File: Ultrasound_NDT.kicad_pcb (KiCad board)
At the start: 4 copper layers, 396 parts, among them J1 Conn_01x02_Pin, J10 CONSMA002-SMD, J11 Logger Connector, J12 UART Connector, J13 External UART, J14 External I2C, J15 JTAG Header, J16 External Power Connector, J17 Input Power, J18 Conn_01x02_Pin, J19 Conn_01x02_Pin, J2 Conn_01x02_Pin, J20 Conn_01x02_Pin, J21 Conn_01x02_Pin, J22 Conn_01x02_Pin, J23 Conn_01x02_Pin, J24 Conn_01x02_Pin, J25 Conn_01x02_Pin, J26 Spectrography Power, J27 Conn_01x02_Pin, J3 CONSMA002-SMD, J4 CONSMA002-SMD, J5 CONSMA002-SMD, J6 CONSMA002-SMD, J7 CONSMA002-SMD, J8 CONSMA002-SMD, J9 CONSMA002-SMD, SW1 XRSn_button, U1 AD8334ACPZ, U10 TLV9354IDR, U11 TLV9354IDR, U12 TPS63700DRCR, U13 M24M01E-FMN6TP, U14 LDL212PU50R, U15 AZ1117CH2-3.3, U16 AZ1117CH2-3.3, U17 TRS3221EIPWR, U2 DSC1001DI2-125.0000T, U3 MAX14808ETK_, U4 AD8334ACPZ, U5 F280025PNS, U6 REF3030, U7 MIC920YC5-TR, U8 TLV9354IDR, U9 TLV9354IDR, Y2 H130B-16.000-18-3030-EXT-TR

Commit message: finished 70% of the layout, only power is remaining + matching parts with each other (analog)
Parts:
- removed TP1, TP17, TP18, TP19, TP2, TP20, TP21, TP22, TP23, TP24, TP25, TP26, TP27, TP28, TP29, TP3, TP30, TP31, TP32, TP33, TP34, TP35, TP36, TP37, TP38, TP39, TP4, TP40, TP41, TP42, TP43, TP44, TP45, TP46, TP47, TP48, TP49, TP5, TP50, TP51, TP52, TP53, TP54, TP55, TP56, TP57, TP58, TP59, TP6, TP60, TP61, TP62, TP63, TP64, TP65, TP66, TP67, TP68, TP69, TP7, TP70, TP71, TP72, TP73, TP74, TP75, TP76, TP77, TP78, TP79, TP8, TP80, TP81: RCT-0C, digikey-footprints:PROBE_PAD_0805
- removed TP10, TP11, TP12, TP13, TP14, TP15, TP16, TP9: TestPoint, TestPoint:TestPoint_Pad_D1.5mm
- C10, C11, C112, C113, C12, C13, C16, C17, C18, C19, C2, C20, C21, C22, C23, C24, C25, C29, C3, C31, C32, C33, C34, C35, C36, C37, C38, C39, C4, C40, C41, C42, C43, C44, C45, C46, C5, C57, C6, C60, C63, C66, C69, C7, C72, C73, C74, C8, C9: moved to B.Cu
- moved C68 289.4 mm to (169.8, 241.5), turned to 90 degrees
- moved C66 287.1 mm to (172.2, 215.4), turned to 90 degrees
- moved C63 286.6 mm to (171.7, 212.4), turned to -90 degrees
- moved C74 283.1 mm to (170.2, 217.6), turned to 90 degrees
- moved R41 282.7 mm to (167.8, 241.7), turned to -90 degrees
- moved C73 282.5 mm to (169.7, 214.4), turned to -45 degrees
- moved C67 281.9 mm to (161.0, 242.4), turned to 90 degrees
- moved R40 275.4 mm to (159.0, 242.6), turned to -90 degrees
- moved C57 272.3 mm to (155.5, 215.4), turned to 90 degrees
- moved C69 271.9 mm to (157.7, 217.9), turned to 90 degrees
- moved C60 271.6 mm to (156.0, 212.3), turned to -90 degrees
- moved C72 271.2 mm to (158.0, 214.6), turned to -135 degrees
- moved R104 269.1 mm to (171.0, 223.1), turned to 180 degrees
- moved R42 265.6 mm to (156.0, 223.1)
- moved R43 264.7 mm to (156.0, 221.6)
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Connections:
- J15 pad 4: /Main MCU Section/JTAG_TDO -> /Main MCU Section/JTAG_TMS
- J15 pad 5: /Main MCU Section/JTAG_TCK -> /Main MCU Section/JTAG_TDO
- J15 pad 6: /Main MCU Section/JTAG_TMS -> /Main MCU Section/JTAG_TCK
- R10 pad 1: /Main MCU Section/CH7_A -> /Main MCU Section/CH7_A_MCU
- R11 pad 1: /Main MCU Section/CH5_A -> /Main MCU Section/CH5_A_MCU
- R12 pad 1: /Main MCU Section/CH1_A -> /Main MCU Section/CH1_A_MCU
- R13 pad 1: /Main MCU Section/CH1_B -> /Main MCU Section/CH1_B_MCU
- R14 pad 1: /Main MCU Section/CH2_A -> /Main MCU Section/CH2_A_MCU
- R15 pad 1: /Main MCU Section/CH2_B -> /Main MCU Section/CH2_B_MCU
- R16 pad 1: /Main MCU Section/CH3_A -> /Main MCU Section/CH3_A_MCU
- R17 pad 1: /Main MCU Section/CH3_B -> /Main MCU Section/CH3_B_MCU
- R18 pad 1: /Main MCU Section/CH4_A -> /Main MCU Section/CH4_A_MCU
- R19 pad 1: /Main MCU Section/CH4_B -> /Main MCU Section/CH4_B_MCU
- R4 pad 1: /Main MCU Section/CH5_B -> /Main MCU Section/CH5_B_MCU
- R5 pad 1: /Main MCU Section/CH8_B -> /Main MCU Section/CH8_B_MCU
- R6 pad 1: /Main MCU Section/CH6_A -> /Main MCU Section/CH6_A_MCU
- R7 pad 1: /Main MCU Section/CH6_B -> /Main MCU Section/CH6_B_MCU
- R8 pad 1: /Main MCU Section/CH8_A -> /Main MCU Section/CH8_A_MCU
- R9 pad 1: /Main MCU Section/CH7_B -> /Main MCU Section/CH7_B_MCU
- U5 pad 62: /Main MCU Section/CH5_A -> /Main MCU Section/CH5_A_MCU
- U5 pad 63: /Main MCU Section/CH5_B -> /Main MCU Section/CH5_B_MCU
- U5 pad 64: /Main MCU Section/CH6_A -> /Main MCU Section/CH6_A_MCU
- U5 pad 65: /Main MCU Section/CH6_B -> /Main MCU Section/CH6_B_MCU
- U5 pad 66: /Main MCU Section/CH7_A -> /Main MCU Section/CH7_A_MCU
- U5 pad 67: /Main MCU Section/CH7_B -> /Main MCU Section/CH7_B_MCU
- U5 pad 68: /Main MCU Section/CH8_A -> /Main MCU Section/CH8_A_MCU
- U5 pad 69: /Main MCU Section/CH8_B -> /Main MCU Section/CH8_B_MCU
- U5 pad 73: /Main MCU Section/CH4_B -> /Main MCU Section/CH4_B_MCU
- U5 pad 74: /Main MCU Section/CH4_A -> /Main MCU Section/CH4_A_MCU
- U5 pad 75: /Main MCU Section/CH3_B -> /Main MCU Section/CH3_B_MCU
- U5 pad 76: /Main MCU Section/CH3_A -> /Main MCU Section/CH3_A_MCU
- U5 pad 77: /Main MCU Section/CH2_B -> /Main MCU Section/CH2_B_MCU
- U5 pad 78: /Main MCU Section/CH2_A -> /Main MCU Section/CH2_A_MCU
- U5 pad 79: /Main MCU Section/CH1_B -> /Main MCU Section/CH1_B_MCU
- U5 pad 80: /Main MCU Section/CH1_A -> /Main MCU Section/CH1_A_MCU

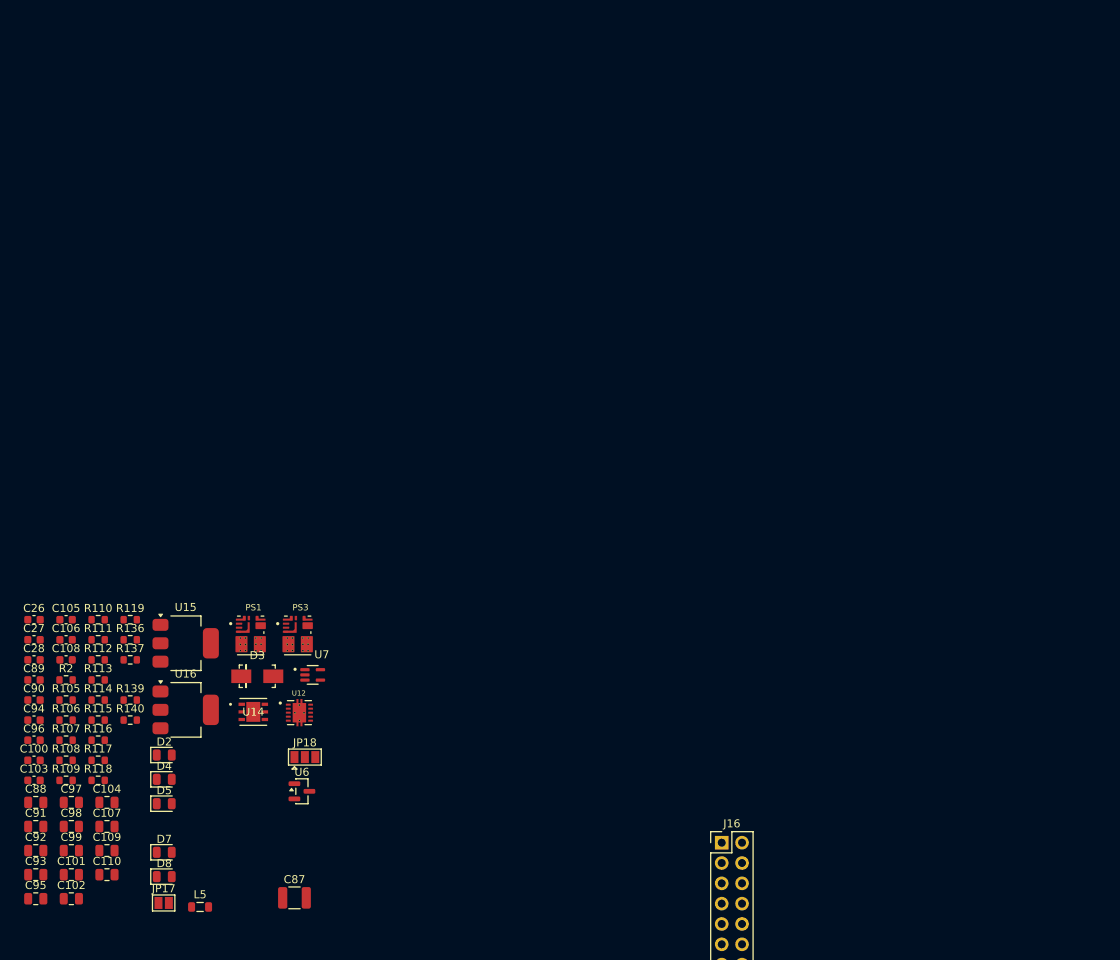
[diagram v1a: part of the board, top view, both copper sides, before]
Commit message: finished laying out all individual blocks, integration comes next, updated schematic
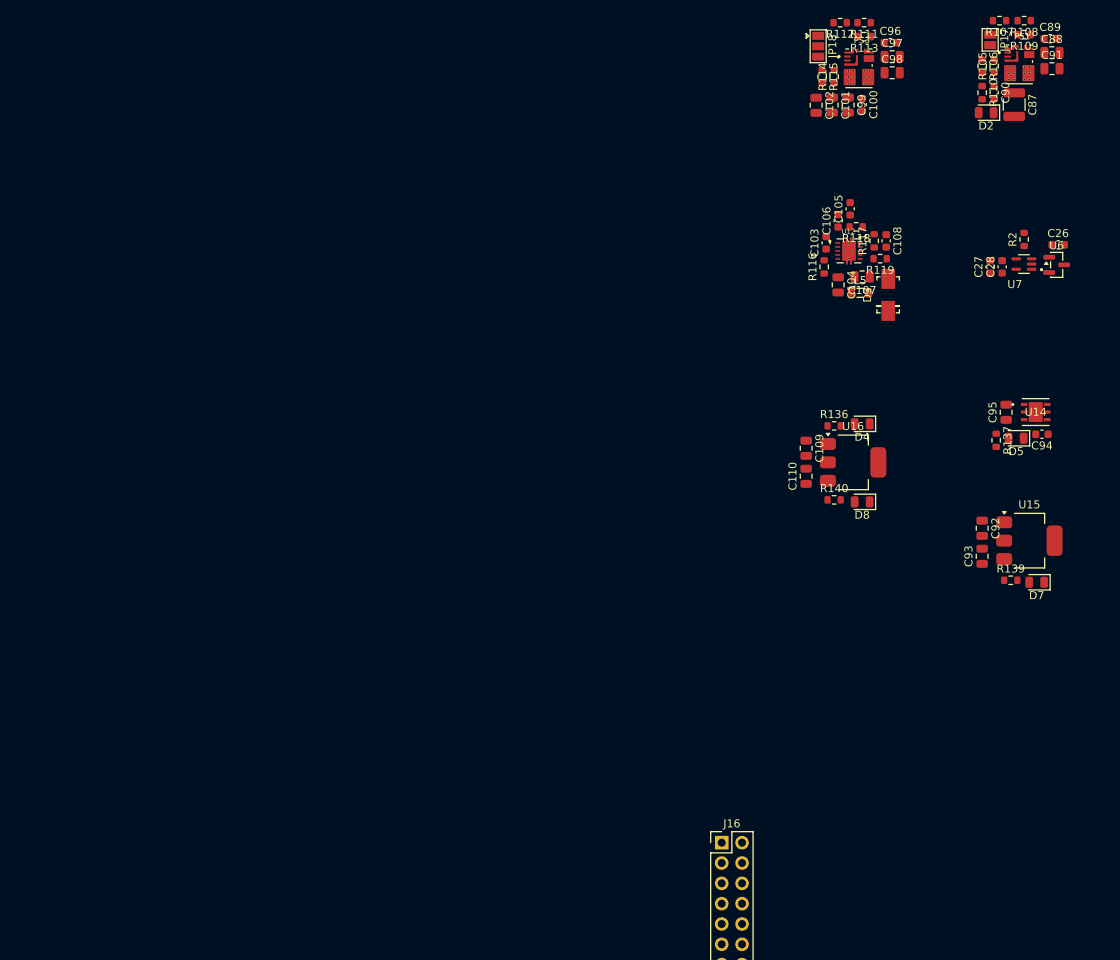
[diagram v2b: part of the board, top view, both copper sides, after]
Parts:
- moved C91 158.5 mm to (-30.8, 24.0)
- moved C88 157.9 mm to (-30.8, 22.0)
- moved R109 151.8 mm to (-34.2, 19.8), turned to 180 degrees
- moved R108 151.3 mm to (-34.2, 18.0), turned to 180 degrees
- moved C89 150.2 mm to (-31.0, 20.2)
- moved JP17 149.4 mm to (-38.5, 20.4), turned to -90 degrees
- moved R107 147.3 mm to (-37.3, 18.0), turned to 180 degrees
- moved C90 142.0 mm to (-38.0, 27.0), turned to -90 degrees
- moved R106 140.7 mm to (-39.5, 23.7), turned to -90 degrees
- moved R105 140.5 mm to (-38.0, 23.7), turned to 90 degrees
- moved C98 139.3 mm to (-50.8, 24.5)
- moved C97 138.6 mm to (-50.8, 22.5)
- moved C96 138.1 mm to (-51.0, 20.8)
- moved C26 136.3 mm to (-30.0, 46.0)
- moved C102 136.0 mm to (-60.2, 28.6), turned to -90 degrees
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
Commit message: fininshed 90% placement, only power section needs refinement, next sprint the stackup will be decided, probably 6 layers
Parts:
- C100, C101, C102, C103, C104, C105, C106, C107, C108, C109, C110, C26, C27, C28, C87, C88, C89, C90, C91, C92, C93, C94, C95, C96, C97, C98, C99, D2, D3, D4, D5, D6, D7, D8, J17, J26, JP17, JP18, L5, PS1, PS3, R10, R105, R106, R107, R108, R109, R11, R110, R111, R112, R113, R114, R115, R116, R117, R118, R119, R12, R128, R129, R13, R130, R131, R132, R133, R134, R135, R136, R137, R138, R139, R14, R140, R15, R16, R17, R18, R19, R2, R4, R5, R6, R7, R8, R9, U12, U14, U15, U16, U6, U7: moved to B.Cu
- moved J17 259.7 mm to (116.1, 173.8), turned to 180 degrees
- moved D6 253.4 mm to (122.4, 167.0), turned to 180 degrees
- moved J26 250.3 mm to (115.1, 167.0), turned to 90 degrees
- moved R138 249.5 mm to (118.9, 167.0)
- moved R111 219.4 mm to (109.4, 164.4)
- moved R112 219.4 mm to (106.4, 164.4)
- moved R113 217.1 mm to (109.4, 162.7)
- moved C96 216.1 mm to (112.6, 161.9)
- moved JP18 215.5 mm to (103.6, 161.5), turned to 90 degrees
- moved R107 214.5 mm to (119.3, 164.5)
- moved R108 214.5 mm to (122.4, 164.5)
- moved C97 213.9 mm to (112.9, 160.2)
- moved R109 212.1 mm to (122.4, 162.8)
- moved PS3 212.0 mm to (108.7, 158.7)
- moved C89 211.4 mm to (125.6, 162.3)
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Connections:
- C35 pad 1: /Receiving Section/TR_OUT1 -> /Receiving Section/TR_OUT4
- C36 pad 1: /Receiving Section/TR_OUT2 -> /Receiving Section/TR_OUT1
- C37 pad 1: /Receiving Section/TR_OUT3 -> /Receiving Section/TR_OUT2
- C38 pad 1: /Receiving Section/TR_OUT4 -> /Receiving Section/TR_OUT3
- C57 pad 1: /Receiving Section/TR_OUT5 -> /Receiving Section/TR_OUT8
- C60 pad 1: /Receiving Section/TR_OUT6 -> /Receiving Section/TR_OUT5
- C63 pad 1: /Receiving Section/TR_OUT7 -> /Receiving Section/TR_OUT6
- C66 pad 1: /Receiving Section/TR_OUT8 -> /Receiving Section/TR_OUT7
- J15 pad 4: /Main MCU Section/JTAG_TMS -> /Main MCU Section/JTAG_TDO
- J15 pad 5: /Main MCU Section/JTAG_TDO -> /Main MCU Section/JTAG_TCK
- J15 pad 6: /Main MCU Section/JTAG_TCK -> /Main MCU Section/JTAG_TMS
- R32 pad 1: /Receiving Section/TR_OUT4 -> /Receiving Section/TR_OUT3
- R33 pad 1: /Receiving Section/TR_OUT3 -> /Receiving Section/TR_OUT2
- R34 pad 1: /Receiving Section/TR_OUT2 -> /Receiving Section/TR_OUT1
- R35 pad 1: /Receiving Section/TR_OUT1 -> /Receiving Section/TR_OUT4
- R44 pad 1: /Receiving Section/TR_OUT8 -> /Receiving Section/TR_OUT7
- R45 pad 1: /Receiving Section/TR_OUT7 -> /Receiving Section/TR_OUT6
- R46 pad 1: /Receiving Section/TR_OUT6 -> /Receiving Section/TR_OUT5
- R47 pad 1: /Receiving Section/TR_OUT5 -> /Receiving Section/TR_OUT8
- U1 pad 1: /Receiving Section/TR_OUT6 -> /Receiving Section/TR_OUT5
- U1 pad 16: /Receiving Section/TR_OUT7 -> /Receiving Section/TR_OUT6
- U1 pad 19: /Receiving Section/TR_OUT8 -> /Receiving Section/TR_OUT7
- U1 pad 62: /Receiving Section/TR_OUT5 -> /Receiving Section/TR_OUT8
- U4 pad 1: /Receiving Section/TR_OUT2 -> /Receiving Section/TR_OUT1
- U4 pad 16: /Receiving Section/TR_OUT3 -> /Receiving Section/TR_OUT2
- U4 pad 19: /Receiving Section/TR_OUT4 -> /Receiving Section/TR_OUT3
- U4 pad 62: /Receiving Section/TR_OUT1 -> /Receiving Section/TR_OUT4
- U5 pad 69: /Main MCU Section/CH8_B_MCU -> /Main MCU Section/CH8_B
- U5 pad 73: /Main MCU Section/CH4_B_MCU -> /Main MCU Section/CH4_B
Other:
- board text added: "Split this header into 2 separate headers."

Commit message: Finished placement & started routing, check on stackup & see routing & sigal integrity videos downloaded
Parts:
- added J28: Conn_02x04_Odd_Even, Connector_PinHeader_2.54mm:PinHeader_2x04_P2.54mm_Vertical, F.Cu at (127.0, 61.4)
- C47, C48, C67, C68, L1, L2, L3, L4, R38, R39, R40, R41: moved to B.Cu
- J16: value External Power Connector -> Conn_02x04_Odd_Even; footprint Connector_PinHeader_2.54mm:PinHeader_2x08_P2.54mm_Vertical -> Connector_PinHeader_2.54mm:PinHeader_2x04_P2.54mm_Vertical
- moved J17 119.6 mm to (64.8, 65.8), turned to 90 degrees
- moved R112 110.1 mm to (70.6, 60.4), turned to 90 degrees
- moved R111 108.3 mm to (70.6, 63.4), turned to 90 degrees
- moved JP18 108.2 mm to (73.5, 57.6), turned to 0 degrees
- moved J26 107.8 mm to (65.0, 71.6), turned to 180 degrees
- moved R138 107.1 mm to (68.0, 72.9), turned to -90 degrees
- moved R113 106.0 mm to (72.3, 63.4), turned to 90 degrees
- moved D6 105.8 mm to (68.0, 76.4), turned to 90 degrees
- moved R115 104.6 mm to (77.3, 56.1), turned to 0 degrees
- moved R107 103.5 mm to (70.5, 73.3), turned to 90 degrees
- moved R114 103.5 mm to (77.3, 57.6), turned to 180 degrees
- moved C96 103.2 mm to (73.1, 66.6), turned to -90 degrees
- moved R108 102.3 mm to (70.5, 76.4), turned to 90 degrees
- moved C110 102.2 mm to (82.0, 52.1), turned to -90 degrees
- moved C101 101.9 mm to (77.6, 59.4), turned to 180 degrees
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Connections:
- R128 pad 2: /Receiving Section/TR_OUT6 -> /Receiving Section/TR_OUT8
- R130 pad 2: /Receiving Section/TR_OUT2 -> /Receiving Section/TR_OUT4
- R133 pad 1: /Receiving Section/TR_OUT4 -> /Receiving Section/TR_OUT2
- R135 pad 1: /Receiving Section/TR_OUT8 -> /Receiving Section/TR_OUT6
- R85 pad 2: /Pulsing Section/TR2 -> /Pulsing Section/TR4
- R87 pad 2: /Pulsing Section/TR4 -> /Pulsing Section/TR2
- R92 pad 2: /Pulsing Section/TR6 -> /Pulsing Section/TR8
- R97 pad 2: /Pulsing Section/TR8 -> /Pulsing Section/TR6
- U5 pad 1: /Main MCU Section/AFE_GAIN_B1 -> /Main MCU Section/AFE_GAIN_A2
- U5 pad 10: /Main MCU Section/ADC1 -> /Main MCU Section/ADC3
- U5 pad 12: /Main MCU Section/ADC3 -> /Main MCU Section/ADC1
- U5 pad 14: /Main MCU Section/ADC5 -> /Main MCU Section/ADC8
- U5 pad 15: /Main MCU Section/ADC6 -> /Main MCU Section/ADC7
- U5 pad 16: /Main MCU Section/ADC7 -> /Main MCU Section/ADC6
- U5 pad 17: /Main MCU Section/ADC8 -> /Main MCU Section/ADC5
- U5 pad 2: /Main MCU Section/AFE_GAIN_B2 -> /Main MCU Section/AFE_GAIN_A1
- U5 pad 58: /Main MCU Section/AFE_GAIN_A2 -> /Main MCU Section/AFE_GAIN_B2
- U5 pad 59: /Main MCU Section/AFE_GAIN_A1 -> /Main MCU Section/AFE_GAIN_B1
- U5 pad 69: /Main MCU Section/CH8_B -> /Main MCU Section/CH8_B_MCU
- U5 pad 73: /Main MCU Section/CH4_B -> /Main MCU Section/CH4_B_MCU
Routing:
- net /Main MCU Section/CH5_A_MCU: track 0.00 -> 13.4 mm
- net /Main MCU Section/CH5_B_MCU: track 0.00 -> 12.4 mm
- net /Main MCU Section/CH1_A_MCU: track 0.00 -> 11.7 mm
- net /Main MCU Section/CH6_A_MCU: track 0.00 -> 11.3 mm
- net /Main MCU Section/CH1_B_MCU: track 0.00 -> 10.9 mm
- net /Main MCU Section/CH2_A_MCU: track 0.00 -> 10.2 mm
- net /Main MCU Section/CH6_B_MCU: track 0.00 -> 9.75 mm
- net /Main MCU Section/CH2_B_MCU: track 0.00 -> 9.38 mm
- net /Main MCU Section/CH7_A_MCU: track 0.00 -> 9.00 mm
- net /Main MCU Section/CH3_A_MCU: track 0.00 -> 8.82 mm
- net /Main MCU Section/CH7_B_MCU: track 0.00 -> 7.86 mm
- net /Main MCU Section/CH3_B_MCU: track 0.00 -> 7.75 mm
- net /Main MCU Section/CH8_A_MCU: track 0.00 -> 7.44 mm
- net /Main MCU Section/CH4_A_MCU: track 0.00 -> 7.34 mm
- net /Main MCU Section/CH4_B_MCU: track 0.00 -> 7.17 mm
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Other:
- board outline added: 100 x 100 mm
- copper layers 4 -> 6
- board text removed: "Split this header into 2 separate headers."

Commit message: started routing, finished 15%
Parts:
- C115, R49, R50: moved to B.Cu
- R10, R11, R12, R13, R14, R15, R16, R17, R18, R19, R4, R5, R6, R7, R8, R9: moved to F.Cu
- moved R49 7.55 mm to (112.2, 76.2), turned to -90 degrees
- moved R50 7.05 mm to (113.8, 76.2), turned to -90 degrees
- moved C14 4.72 mm to (128.5, 99.2), turned to 0 degrees
- moved R11 4.26 mm to (121.8, 80.8)
- moved R12 4.20 mm to (104.0, 80.8)
- moved R20 3.54 mm to (153.0, 111.0), turned to 90 degrees
- moved R6 3.48 mm to (119.8, 80.8)
- moved R14 3.41 mm to (106.0, 80.8)
- moved R13 3.07 mm to (105.0, 83.8)
- moved R4 3.05 mm to (120.8, 83.8)
- moved R22 2.96 mm to (153.0, 114.2), turned to -90 degrees
- moved R10 2.85 mm to (117.8, 80.8)
- moved R16 2.77 mm to (108.0, 80.8)
- moved R1 2.69 mm to (125.4, 99.2), turned to 0 degrees
- moved R8 2.48 mm to (115.8, 80.8)
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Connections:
- J15 pad 4: /Main MCU Section/JTAG_TDO -> /Main MCU Section/JTAG_TMS
- J15 pad 5: /Main MCU Section/JTAG_TCK -> /Main MCU Section/JTAG_TDO
- J15 pad 6: /Main MCU Section/JTAG_TMS -> /Main MCU Section/JTAG_TCK
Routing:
- net /Main MCU Section/LINB_RX: track 0.00 -> 47.3 mm
- net /Main MCU Section/JTAG_TDO: track 0.00 -> 45.9 mm, vias 0 -> 1
- net /Pulsing Section/HV_OUT1: track 0.00 -> 45.5 mm
- net /Main MCU Section/LINB_TX: track 0.00 -> 45.0 mm
- net /Pulsing Section/HV_OUT8: track 0.00 -> 44.8 mm
- net /Main MCU Section/JTAG_TMS: track 0.00 -> 44.5 mm, vias 0 -> 1
- net /Main MCU Section/JTAG_TDI: track 0.00 -> 43.3 mm, vias 0 -> 1
- net /Main MCU Section/JTAG_TCK: track 0.00 -> 43.1 mm, vias 0 -> 1
- net /Main MCU Section/I2CB_SDA: track 0.00 -> 40.6 mm, vias 0 -> 1
- net /Main MCU Section/I2CB_SCL: track 0.00 -> 38.9 mm, vias 0 -> 1
- net /Pulsing Section/HV_OUT7: track 0.00 -> 37.2 mm
- net /Pulsing Section/HV_OUT2: track 0.00 -> 36.8 mm
- net /Main MCU Section/CH8_B: track 0.00 -> 30.2 mm, vias 0 -> 2
- net /Main MCU Section/CH4_B: track 0.00 -> 30.1 mm, vias 0 -> 2
- net /Pulsing Section/HV_OUT3: track 0.00 -> 29.1 mm
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- added copper zone on In1.Cu, net GND
